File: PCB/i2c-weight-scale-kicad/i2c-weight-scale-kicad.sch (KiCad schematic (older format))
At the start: 4 parts, among them P1 4_STRAIN_GAUGES

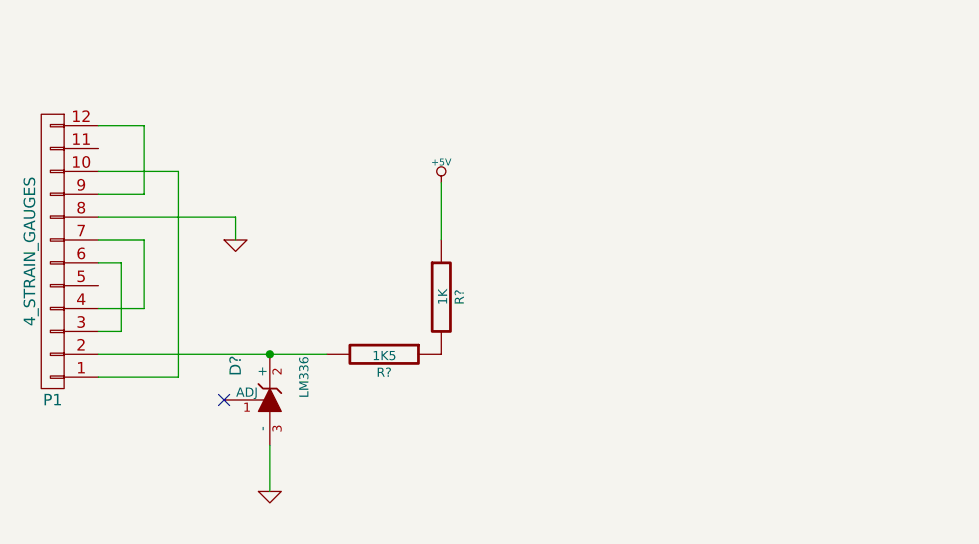
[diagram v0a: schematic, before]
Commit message: Complete the load cell and amplification schematic
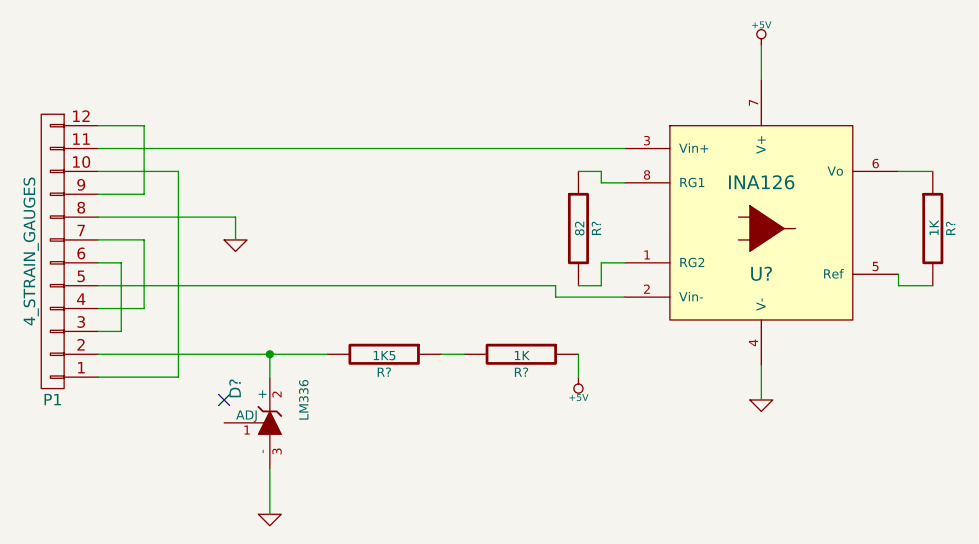
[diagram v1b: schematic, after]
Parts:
- added R?: 82, symbol R
- added R?: 1K, symbol R
- added U?: INA126, symbol INA126
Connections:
- net +5V: now also U?.7 (V+)
- net GND: now also U?.4 (V-)
- net at P1.11 (P11): now also U?.3 (Vin+)
- net at P1.5 (P5): now also U?.2 (Vin-)
- new net: R?.2, U?.1 (RG2)
- new net: R?.2, U?.5 (Ref)
- new net: R?.1, U?.6 (Vo)
- new net: R?.1, U?.8 (RG1)
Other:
- moved on the sheet: D?, R?
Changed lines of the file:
@@
 L LM336 D?
 U 1 1 547BA8E5
-P 3050 2500
-F 0 "D?" H 3200 2650 50  0000 C CNN
-F 1 "LM336" H 3150 2350 40  0000 C CNN
-F 2 "" H 3050 2500 60  0000 C CNN
-F 3 "" H 3050 2500 60  0000 C CNN
-	1    3050 2500
+P 3050 2600
+F 0 "D?" H 3200 2750 50  0000 C CNN
+F 1 "LM336" H 3150 2450 40  0000 C CNN
+F 2 "" H 3050 2600 60  0000 C CNN
+F 3 "" H 3050 2600 60  0000 C CNN
+	1    3050 2600
 	0    -1   -1   0
 $EndComp
@@
 L GND #PWR?
 U 1 1 547BA9CA
-P 3050 2900
-F 0 "#PWR?" H 3050 2900 30  0001 C CNN
-F 1 "GND" H 3050 2830 30  0001 C CNN
-F 2 "" H 3050 2900 60  0000 C CNN
-F 3 "" H 3050 2900 60  0000 C CNN
-	1    3050 2900
+P 3050 3000
+F 0 "#PWR?" H 3050 3000 30  0001 C CNN
+F 1 "GND" H 3050 2930 30  0001 C CNN
+F 2 "" H 3050 3000 60  0000 C CNN
+F 3 "" H 3050 3000 60  0000 C CNN
+	1    3050 3000
 	1    0    0    -1
 $EndComp
-Wire Wire Line
-	3050 2900 3050 2700
 $Comp
 L +5V #PWR?
 U 1 1 547BAA03
-P 3800 1550
-F 0 "#PWR?" H 3800 1640 20  0001 C CNN
-F 1 "+5V" H 3800 1640 30  0000 C CNN
-F 2 "" H 3800 1550 60  0000 C CNN
-F 3 "" H 3800 1550 60  0000 C CNN
-	1    3800 1550
-	1    0    0    -1
+P 4400 2400
+F 0 "#PWR?" H 4400 2490 20  0001 C CNN
+F 1 "+5V" H 4400 2490 30  0000 C CNN
+F 2 "" H 4400 2400 60  0000 C CNN
+F 3 "" H 4400 2400 60  0000 C CNN
+	1    4400 2400
+	-1   0    0    1
 $EndComp
 $Comp
 L R R?
 U 1 1 547BAA17
-P 3800 2050
-F 0 "R?" V 3880 2050 40  0000 C CNN
-F 1 "1K" V 3807 2051 40  0000 C CNN
-F 2 "" V 3730 2050 30  0000 C CNN
-F 3 "" H 3800 2050 30  0000 C CNN
-	1    3800 2050
-	1    0    0    -1
+P 4150 2300
+F 0 "R?" V 4230 2300 40  0000 C CNN
+F 1 "1K" V 4157 2301 40  0000 C CNN
+F 2 "" V 4080 2300 30  0000 C CNN
+F 3 "" H 4150 2300 30  0000 C CNN
+	1    4150 2300
+	0    1    1    0
 $EndComp
 $Comp
@@
 	0    1    1    0
 $EndComp
+Connection ~ 3050 2300
 Wire Wire Line
-	3800 1550 3800 1800
-Connection ~ 3050 2300
+	3050 2800 3050 3000
+Wire Wire Line
+	3050 2400 3050 2300
+$Comp
+L INA126 U?
+U 1 1 5480C719
+P 5200 1750
+F 0 "U?" H 5200 1550 60  0000 C CNN
+F 1 "INA126" H 5200 1950 60  0000 C CNN
+F 2 "" H 5250 1750 60  0000 C CNN
+F 3 "" H 5250 1750 60  0000 C CNN
+	1    5200 1750
+	1    0    0    -1
+$EndComp
+Wire Wire Line
+	3800 2300 3900 2300
+Wire Wire Line
+	4400 2400 4400 2300
+$Comp
+L GND #PWR?
+U 1 1 5480CA2A
+P 5200 2500
+F 0 "#PWR?" H 5200 2500 30  0001 C CNN
+F 1 "GND" H 5200 2430 30  0001 C CNN
+F 2 "" H 5200 2500 60  0000 C CNN
+F 3 "" H 5200 2500 60  0000 C CNN
+	1    5200 2500
+	1    0    0    -1
+$EndComp
+Wire Wire Line
+	5200 2350 5200 2500
+$Comp
+L +5V #PWR?
+U 1 1 5480CA59
+P 5200 950
+F 0 "#PWR?" H 5200 1040 20  0001 C CNN
+F 1 "+5V" H 5200 1040 30  0000 C CNN
+F 2 "" H 5200 950 60  0000 C CNN
+F 3 "" H 5200 950 60  0000 C CNN
+	1    5200 950
+	1    0    0    -1
+$EndComp
+Wire Wire Line
+	5200 950  5200 1100
+$Comp
+L R R?
+U 1 1 5480CF0C
+P 4400 1750
+F 0 "R?" V 4480 1750 40  0000 C CNN
+F 1 "82" V 4407 1751 40  0000 C CNN
+F 2 "" V 4330 1750 30  0000 C CNN
+F 3 "" H 4400 1750 30  0000 C CNN
+	1    4400 1750
+	1    0    0    -1
+$EndComp
+Wire Wire Line
+	4400 1500 4500 1500
+Wire Wire Line
+	4500 1500 4500 1550
+Wire Wire Line
+	4500 1550 4600 1550
+Wire Wire Line
+	4400 2000 4500 2000
+Wire Wire Line
+	4500 2000 4500 1900
+Wire Wire Line
+	4500 1900 4600 1900
+Wire Wire Line
+	2300 2000 4300 2000
+Wire Wire Line
+	4300 2000 4300 2050
+Wire Wire Line
+	4300 2050 4600 2050
+Wire Wire Line
+	2300 1400 4600 1400
+$Comp
+L R R?
+U 1 1 5480CFE5
+P 5950 1750
+F 0 "R?" V 6030 1750 40  0000 C CNN
+F 1 "1K" V 5957 1751 40  0000 C CNN
+F 2 "" V 5880 1750 30  0000 C CNN
+F 3 "" H 5950 1750 30  0000 C CNN
+	1    5950 1750
+	1    0    0    -1
+$EndComp
+Wire Wire Line
+	5950 1500 5800 1500
+Wire Wire Line
+	5950 2000 5800 2000
+Wire Wire Line
+	5800 2000 5800 1950
 $EndSCHEMATC

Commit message: Add RJ14 and PIC12F1822 components
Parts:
- added J?: I2C_RJ14, symbol I2C_RJ14
- added U?: PIC12F1822, symbol PIC12F1822
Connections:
- net +5V: now also J?.2 (VSS), U?.1 (VDD)
- net GND: now also R?.2, U?.5 (Ref), J?.1 (VDD), U?.8 (VSS)
- net at R?.1, U?.6 (Vo): now also U?.3 (RA4/AN3)
- new net: J?.3 (SDA), U?.5 (RA2/AN2/SDA)
- new net: J?.4 (SCL), U?.6 (RA1/AN1/SCL/ICSPCLK)
- no-connect marks 1 -> 3
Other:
- moved on the sheet: D?, P1, R?, U?

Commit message: Tweak electrical type to pass the electrical rule check
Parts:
- added R5: 10K, symbol R
- gave numbers to parts that had none: 8
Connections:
- net +5V: now also R5.2
- net at U2.4 (RA3/~MCLR): now also R5.1
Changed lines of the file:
@@
 	2550 3050 2550 3150
 $Comp
-L LM336 D?
+L LM336 D1
 U 1 1 547BA8E5
 P 2700 3950
-F 0 "D?" H 2850 4100 50  0000 C CNN
+F 0 "D1" H 2850 4100 50  0000 C CNN
 F 1 "LM336" H 2800 3800 40  0000 C CNN
 F 2 "" H 2700 3950 60  0000 C CNN
@@
 $EndComp
 $Comp
-L R R?
+L R R2
 U 1 1 547BAA17
 P 3800 3650
-F 0 "R?" V 3880 3650 40  0000 C CNN
+F 0 "R2" V 3880 3650 40  0000 C CNN
 F 1 "1K" V 3807 3651 40  0000 C CNN
 F 2 "" V 3730 3650 30  0000 C CNN
@@
 $EndComp
 $Comp
-L R R?
+L R R1
 U 1 1 547BAA9F
 P 3200 3650
-F 0 "R?" V 3280 3650 40  0000 C CNN
+F 0 "R1" V 3280 3650 40  0000 C CNN
 F 1 "1K5" V 3207 3651 40  0000 C CNN
 F 2 "" V 3130 3650 30  0000 C CNN
@@
 	2700 3750 2700 3650
 $Comp
-L INA126 U?
+L INA126 U1
 U 1 1 5480C719
 P 4850 3100
-F 0 "U?" H 4850 2900 60  0000 C CNN
+F 0 "U1" H 4850 2900 60  0000 C CNN
 F 1 "INA126" H 4850 3300 60  0000 C CNN
 F 2 "" H 4900 3100 60  0000 C CNN
@@
 	4850 3700 4850 3850
 $Comp
-L +5V #PWR05
-U 1 1 5480CA59
-P 4850 2300
-F 0 "#PWR05" H 4850 2390 20  0001 C CNN
-F 1 "+5V" H 4850 2390 30  0000 C CNN
-F 2 "" H 4850 2300 60  0000 C CNN
-F 3 "" H 4850 2300 60  0000 C CNN
-	1    4850 2300
-	1    0    0    -1
-$EndComp
-Wire Wire Line
-	4850 2300 4850 2450
-$Comp
-L R R?
+L R R3
 U 1 1 5480CF0C
 P 4050 3100
-F 0 "R?" V 4130 3100 40  0000 C CNN
+F 0 "R3" V 4130 3100 40  0000 C CNN
 F 1 "82" V 4057 3101 40  0000 C CNN
 F 2 "" V 3980 3100 30  0000 C CNN
@@
 	1950 2750 4250 2750
 $Comp
-L R R?
+L R R4
 U 1 1 5480CFE5
 P 5600 3100
-F 0 "R?" V 5680 3100 40  0000 C CNN
+F 0 "R4" V 5680 3100 40  0000 C CNN
 F 1 "1K" V 5607 3101 40  0000 C CNN
 F 2 "" V 5530 3100 30  0000 C CNN
@@
 NoConn ~ 2500 3950
 $Comp
-L PIC12F1822 U?
+L PIC12F1822 U2
 U 1 1 5480DD29
 P 7450 3100
-F 0 "U?" H 7450 2800 39  0000 C CNN
+F 0 "U2" H 7450 2800 39  0000 C CNN
 F 1 "PIC12F1822" H 7450 3500 39  0000 C CNN
 F 2 "" H 7450 3100 60  0000 C CNN
@@
 $EndComp
 $Comp
-L +5V #PWR06
+L +5V #PWR05
 U 1 1 5480E008
 P 8200 2800
-F 0 "#PWR06" H 8200 2890 20  0001 C CNN
+F 0 "#PWR05" H 8200 2890 20  0001 C CNN
 F 1 "+5V" H 8200 2890 30  0000 C CNN
 F 2 "" H 8200 2800 60  0000 C CNN
@@
 	8200 2800 8000 2800
 $Comp
-L GND #PWR07
+L GND #PWR06
 U 1 1 5480E049
 P 8250 3350
-F 0 "#PWR07" H 8250 3350 30  0001 C CNN
+F 0 "#PWR06" H 8250 3350 30  0001 C CNN
 F 1 "GND" H 8250 3280 30  0001 C CNN
 F 2 "" H 8250 3350 60  0000 C CNN
@@
 	8250 3300 8250 3350
 $Comp
-L GND #PWR08
+L GND #PWR07
 U 1 1 5480E276
 P 5600 3850
-F 0 "#PWR08" H 5600 3850 30  0001 C CNN
+F 0 "#PWR07" H 5600 3850 30  0001 C CNN
 F 1 "GND" H 5600 3780 30  0001 C CNN
 F 2 "" H 5600 3850 60  0000 C CNN
@@
 Connection ~ 5600 2850
 $Comp
-L I2C_RJ14 J?
+L I2C_RJ14 J1
 U 1 1 5480F094
 P 6050 2050
-F 0 "J?" H 6550 2850 60  0000 C CNN
+F 0 "J1" H 6550 2850 60  0000 C CNN
 F 1 "I2C_RJ14" H 6200 2850 60  0000 C CNN
 F 2 "" H 7450 2450 60  0000 C CNN
@@
 $EndComp
 $Comp
-L GND #PWR?
+L GND #PWR08
 U 1 1 5480F671
 P 6600 2350
-F 0 "#PWR?" H 6600 2350 30  0001 C CNN
+F 0 "#PWR08" H 6600 2350 30  0001 C CNN
 F 1 "GND" H 6600 2280 30  0001 C CNN
 F 2 "" H 6600 2350 60  0000 C CNN
@@
 $EndComp
 $Comp
-L +5V #PWR?
+L +5V #PWR09
 U 1 1 5480F697
 P 6450 2300
-F 0 "#PWR?" H 6450 2390 20  0001 C CNN
+F 0 "#PWR09" H 6450 2390 20  0001 C CNN
 F 1 "+5V" H 6450 2390 30  0000 C CNN
 F 2 "" H 6450 2300 60  0000 C CNN
@@
 	6450 2300 6450 2200
 Wire Wire Line
-	6600 2350 6600 2200
-Wire Wire Line
 	6900 3000 6300 3000
 Wire Wire Line
@@
 NoConn ~ 6900 3300
 NoConn ~ 6900 2800
+$Comp
+L R R5
+U 1 1 5480FBAB
+P 6700 3700
+F 0 "R5" V 6780 3700 40  0000 C CNN
+F 1 "10K" V 6707 3701 40  0000 C CNN
+F 2 "" V 6630 3700 30  0000 C CNN
+F 3 "" H 6700 3700 30  0000 C CNN
+	1    6700 3700
+	1    0    0    -1
+$EndComp
+Wire Wire Line
+	6700 3450 6700 3100
+Wire Wire Line
+	6700 3100 6900 3100
+$Comp
+L +5V #PWR010
+U 1 1 5480FC62
+P 6700 4100
+F 0 "#PWR010" H 6700 4190 20  0001 C CNN
+F 1 "+5V" H 6700 4190 30  0000 C CNN
+F 2 "" H 6700 4100 60  0000 C CNN
+F 3 "" H 6700 4100 60  0000 C CNN
+	1    6700 4100
+	-1   0    0    1
+$EndComp
+$Comp
+L +5V #PWR011
+U 1 1 548102BE
+P 4850 2100
+F 0 "#PWR011" H 4850 2190 20  0001 C CNN
+F 1 "+5V" H 4850 2190 30  0000 C CNN
+F 2 "" H 4850 2100 60  0000 C CNN
+F 3 "" H 4850 2100 60  0000 C CNN
+	1    4850 2100
+	1    0    0    -1
+$EndComp
+Wire Wire Line
+	4850 2100 4850 2450
+Wire Wire Line
+	6700 4100 6700 3950
+Wire Wire Line
+	6600 2200 6600 2350
 $EndSCHEMATC

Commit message: Clean up power pins, use VDD instead of +5V
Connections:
- net GND: now also J1.2 (VSS); no longer J1.1 (VDD)
- net +5V renamed VDD
- net VDD: now also J1.1 (VDD); no longer J1.2 (VSS)
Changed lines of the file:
@@
-$EndComp
-$Comp
-L +5V #PWR03
-U 1 1 547BAA03
-P 4050 3750
-F 0 "#PWR03" H 4050 3840 20  0001 C CNN
-F 1 "+5V" H 4050 3840 30  0000 C CNN
-F 2 "" H 4050 3750 60  0000 C CNN
-F 3 "" H 4050 3750 60  0000 C CNN
-	1    4050 3750
-	-1   0    0    1
 $EndComp
 $Comp
@@
 Wire Wire Line
 	3450 3650 3550 3650
-Wire Wire Line
-	4050 3750 4050 3650
-$Comp
-L GND #PWR04
+$Comp
+L GND #PWR03
 U 1 1 5480CA2A
 P 4850 3850
-F 0 "#PWR04" H 4850 3850 30  0001 C CNN
+F 0 "#PWR03" H 4850 3850 30  0001 C CNN
 F 1 "GND" H 4850 3780 30  0001 C CNN
 F 2 "" H 4850 3850 60  0000 C CNN
@@
 $EndComp
 $Comp
-L +5V #PWR05
-U 1 1 5480E008
-P 8200 2800
-F 0 "#PWR05" H 8200 2890 20  0001 C CNN
-F 1 "+5V" H 8200 2890 30  0000 C CNN
-F 2 "" H 8200 2800 60  0000 C CNN
-F 3 "" H 8200 2800 60  0000 C CNN
-	1    8200 2800
-	0    1    1    0
-$EndComp
-Wire Wire Line
-	8200 2800 8000 2800
-$Comp
-L GND #PWR06
-U 1 1 5480E049
-P 8250 3350
-F 0 "#PWR06" H 8250 3350 30  0001 C CNN
-F 1 "GND" H 8250 3280 30  0001 C CNN
-F 2 "" H 8250 3350 60  0000 C CNN
-F 3 "" H 8250 3350 60  0000 C CNN
-	1    8250 3350
-	1    0    0    -1
-$EndComp
-Wire Wire Line
-	8250 3300 8000 3300
-Wire Wire Line
-	8250 3300 8250 3350
-$Comp
-L GND #PWR07
+L GND #PWR04
 U 1 1 5480E276
 P 5600 3850
-F 0 "#PWR07" H 5600 3850 30  0001 C CNN
+F 0 "#PWR04" H 5600 3850 30  0001 C CNN
 F 1 "GND" H 5600 3780 30  0001 C CNN
 F 2 "" H 5600 3850 60  0000 C CNN
@@
 	5850 3200 5850 2850
 Connection ~ 5600 2850
-$Comp
-L I2C_RJ14 J1
-U 1 1 5480F094
-P 6050 2050
-F 0 "J1" H 6550 2850 60  0000 C CNN
-F 1 "I2C_RJ14" H 6200 2850 60  0000 C CNN
-F 2 "" H 7450 2450 60  0000 C CNN
-F 3 "" H 7450 2450 60  0000 C CNN
-	1    6050 2050
-	1    0    0    -1
-$EndComp
-$Comp
-L GND #PWR08
-U 1 1 5480F671
-P 6600 2350
-F 0 "#PWR08" H 6600 2350 30  0001 C CNN
-F 1 "GND" H 6600 2280 30  0001 C CNN
-F 2 "" H 6600 2350 60  0000 C CNN
-F 3 "" H 6600 2350 60  0000 C CNN
-	1    6600 2350
-	1    0    0    -1
-$EndComp
-$Comp
-L +5V #PWR09
-U 1 1 5480F697
-P 6450 2300
-F 0 "#PWR09" H 6450 2390 20  0001 C CNN
-F 1 "+5V" H 6450 2390 30  0000 C CNN
-F 2 "" H 6450 2300 60  0000 C CNN
-F 3 "" H 6450 2300 60  0000 C CNN
-	1    6450 2300
-	-1   0    0    1
-$EndComp
-Wire Wire Line
-	6450 2300 6450 2200
-Wire Wire Line
-	6900 3000 6300 3000
-Wire Wire Line
-	6300 3000 6300 2200
-Wire Wire Line
-	6900 2900 6150 2900
-Wire Wire Line
-	6150 2900 6150 2200
 NoConn ~ 6900 3300
 NoConn ~ 6900 2800
@@
 	6700 3100 6900 3100
 $Comp
-L +5V #PWR010
-U 1 1 5480FC62
+L VDD #PWR05
+U 1 1 5482FF68
+P 4150 3650
+F 0 "#PWR05" H 4150 3750 30  0001 C CNN
+F 1 "VDD" H 4150 3760 30  0000 C CNN
+F 2 "" H 4150 3650 60  0000 C CNN
+F 3 "" H 4150 3650 60  0000 C CNN
+	1    4150 3650
+	0    1    1    0
+$EndComp
+Wire Wire Line
+	4050 3650 4150 3650
+$Comp
+L VDD #PWR06
+U 1 1 54830066
+P 4850 2350
+F 0 "#PWR06" H 4850 2450 30  0001 C CNN
+F 1 "VDD" H 4850 2460 30  0000 C CNN
+F 2 "" H 4850 2350 60  0000 C CNN
+F 3 "" H 4850 2350 60  0000 C CNN
+	1    4850 2350
+	1    0    0    -1
+$EndComp
+Wire Wire Line
+	4850 2350 4850 2450
+$Comp
+L VDD #PWR07
+U 1 1 5483013A
+P 8100 2700
+F 0 "#PWR07" H 8100 2800 30  0001 C CNN
+F 1 "VDD" H 8100 2810 30  0000 C CNN
+F 2 "" H 8100 2700 60  0000 C CNN
+F 3 "" H 8100 2700 60  0000 C CNN
+	1    8100 2700
+	1    0    0    -1
+$EndComp
+Wire Wire Line
+	8100 2700 8100 2800
+Wire Wire Line
+	8100 2800 8000 2800
+$Comp
+L GND #PWR08
+U 1 1 548301EC
+P 8100 3400
+F 0 "#PWR08" H 8100 3400 30  0001 C CNN
+F 1 "GND" H 8100 3330 30  0001 C CNN
+F 2 "" H 8100 3400 60  0000 C CNN
+F 3 "" H 8100 3400 60  0000 C CNN
+	1    8100 3400
+	1    0    0    -1
+$EndComp
+Wire Wire Line
+	8100 3400 8100 3300
+Wire Wire Line
+	8100 3300 8000 3300
+$Comp
+L VDD #PWR09
+U 1 1 54830309
 P 6700 4100
-F 0 "#PWR010" H 6700 4190 20  0001 C CNN
-F 1 "+5V" H 6700 4190 30  0000 C CNN
+F 0 "#PWR09" H 6700 4200 30  0001 C CNN
+F 1 "VDD" H 6700 4210 30  0000 C CNN
 F 2 "" H 6700 4100 60  0000 C CNN
 F 3 "" H 6700 4100 60  0000 C CNN
@@
 	-1   0    0    1
 $EndComp
-$Comp
-L +5V #PWR011
-U 1 1 548102BE
-P 4850 2100
-F 0 "#PWR011" H 4850 2190 20  0001 C CNN
-F 1 "+5V" H 4850 2190 30  0000 C CNN
-F 2 "" H 4850 2100 60  0000 C CNN
-F 3 "" H 4850 2100 60  0000 C CNN
-	1    4850 2100
-	1    0    0    -1
-$EndComp
-Wire Wire Line
-	4850 2100 4850 2450
 Wire Wire Line
 	6700 4100 6700 3950
-Wire Wire Line
-	6600 2200 6600 2350
+$Comp
+L I2C_RJ14 J1
+U 1 1 5483054C
+P 6100 2050
+F 0 "J1" H 6600 2850 60  0000 C CNN
+F 1 "I2C_RJ14" H 6250 2850 60  0000 C CNN
+F 2 "" H 7500 2450 60  0000 C CNN
+F 3 "" H 7500 2450 60  0000 C CNN
+	1    6100 2050
+	1    0    0    -1
+$EndComp
+$Comp
+L GND #PWR010
+U 1 1 548305D9
+P 6500 2400
+F 0 "#PWR010" H 6500 2400 30  0001 C CNN
+F 1 "GND" H 6500 2330 30  0001 C CNN
+F 2 "" H 6500 2400 60  0000 C CNN
+F 3 "" H 6500 2400 60  0000 C CNN
+	1    6500 2400
+	1    0    0    -1
+$EndComp
+Wire Wire Line
+	6500 2400 6500 2200
+$Comp
+L VDD #PWR011
+U 1 1 54830627
+P 6650 2350
+F 0 "#PWR011" H 6650 2450 30  0001 C CNN
+F 1 "VDD" H 6650 2460 30  0000 C CNN
+F 2 "" H 6650 2350 60  0000 C CNN
+F 3 "" H 6650 2350 60  0000 C CNN
+	1    6650 2350
+	-1   0    0    1
+$EndComp
+Wire Wire Line
+	6650 2350 6650 2200
+Wire Wire Line
+	6900 2900 6200 2900
+Wire Wire Line
+	6200 2900 6200 2200
+Wire Wire Line
+	6350 2200 6350 3000
+Wire Wire Line
+	6350 3000 6900 3000
 $EndSCHEMATC

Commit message: Assign footprints to resistors and ICs
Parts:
- D1: footprint (none) -> Housings_TO-92:TO-92-Free-molded-wide-oval
- R1, R2, R3, R4, R5: footprint (none) -> Resistors_ThroughHole:Resistor_Vertical_RM5mm
- U1, U2: footprint (none) -> Sockets_DIP:DIP-8__300
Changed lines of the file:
@@
 F 0 "D1" H 2850 4100 50  0000 C CNN
 F 1 "LM336" H 2800 3800 40  0000 C CNN
-F 2 "" H 2700 3950 60  0000 C CNN
+F 2 "Housings_TO-92:TO-92-Free-molded-wide-oval" H 2700 3950 60  0001 C CNN
 F 3 "" H 2700 3950 60  0000 C CNN
 	1    2700 3950
@@
 F 0 "R2" V 3880 3650 40  0000 C CNN
 F 1 "1K" V 3807 3651 40  0000 C CNN
-F 2 "" V 3730 3650 30  0000 C CNN
+F 2 "Resistors_ThroughHole:Resistor_Vertical_RM5mm" V 3730 3650 30  0001 C CNN
 F 3 "" H 3800 3650 30  0000 C CNN
 	1    3800 3650
@@
 F 0 "R1" V 3280 3650 40  0000 C CNN
 F 1 "1K5" V 3207 3651 40  0000 C CNN
-F 2 "" V 3130 3650 30  0000 C CNN
+F 2 "Resistors_ThroughHole:Resistor_Vertical_RM5mm" V 3130 3650 30  0001 C CNN
 F 3 "" H 3200 3650 30  0000 C CNN
 	1    3200 3650
@@
 F 0 "U1" H 4850 2900 60  0000 C CNN
 F 1 "INA126" H 4850 3300 60  0000 C CNN
-F 2 "" H 4900 3100 60  0000 C CNN
+F 2 "Sockets_DIP:DIP-8__300" H 4900 3100 60  0001 C CNN
 F 3 "" H 4900 3100 60  0000 C CNN
 	1    4850 3100
@@
 F 0 "R3" V 4130 3100 40  0000 C CNN
 F 1 "82" V 4057 3101 40  0000 C CNN
-F 2 "" V 3980 3100 30  0000 C CNN
+F 2 "Resistors_ThroughHole:Resistor_Vertical_RM5mm" V 3980 3100 30  0001 C CNN
 F 3 "" H 4050 3100 30  0000 C CNN
 	1    4050 3100
@@
 F 0 "R4" V 5680 3100 40  0000 C CNN
 F 1 "1K" V 5607 3101 40  0000 C CNN
-F 2 "" V 5530 3100 30  0000 C CNN
+F 2 "Resistors_ThroughHole:Resistor_Vertical_RM5mm" V 5530 3100 30  0001 C CNN
 F 3 "" H 5600 3100 30  0000 C CNN
 	1    5600 3100
@@
 F 0 "U2" H 7450 2800 39  0000 C CNN
 F 1 "PIC12F1822" H 7450 3500 39  0000 C CNN
-F 2 "" H 7450 3100 60  0000 C CNN
+F 2 "Sockets_DIP:DIP-8__300" H 7450 3100 60  0001 C CNN
 F 3 "" H 7450 3100 60  0000 C CNN
 	1    7450 3100
@@
 F 0 "R5" V 6780 3700 40  0000 C CNN
 F 1 "10K" V 6707 3701 40  0000 C CNN
-F 2 "" V 6630 3700 30  0000 C CNN
+F 2 "Resistors_ThroughHole:Resistor_Vertical_RM5mm" V 6630 3700 30  0001 C CNN
 F 3 "" H 6700 3700 30  0000 C CNN
 	1    6700 3700
@@
 F 0 "J1" H 6600 2850 60  0000 C CNN
 F 1 "I2C_RJ14" H 6250 2850 60  0000 C CNN
-F 2 "" H 7500 2450 60  0000 C CNN
+F 2 "" H 7500 2450 60  0001 C CNN
 F 3 "" H 7500 2450 60  0000 C CNN
 	1    6100 2050

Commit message: Associate last component with a custom footprint
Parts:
- J1: footprint (none) -> simlun:RJ14_6P4C_right_angle_Molex_95009-7641
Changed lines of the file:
@@
 F 0 "J1" H 6600 2850 60  0000 C CNN
 F 1 "I2C_RJ14" H 6250 2850 60  0000 C CNN
-F 2 "" H 7500 2450 60  0001 C CNN
+F 2 "simlun:RJ14_6P4C_right_angle_Molex_95009-7641" H 7500 2450 60  0001 C CNN
 F 3 "" H 7500 2450 60  0000 C CNN
 	1    6100 2050
